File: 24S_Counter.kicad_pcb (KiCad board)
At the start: 2 copper layers, 0 parts

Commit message: Add unconnected files
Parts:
- added H1: MountingHole, MountingHole:MountingHole_2.2mm_M2, F.Cu at (47.5, 55.0)
- added H2: MountingHole, MountingHole:MountingHole_2.2mm_M2, F.Cu at (128.5, 55.0)
- added H3: MountingHole, MountingHole:MountingHole_2.2mm_M2, F.Cu at (47.5, 125.5)
- added H4: MountingHole, MountingHole:MountingHole_2.2mm_M2, F.Cu at (128.5, 125.5)
- added J1: +5V, my_footprints:Terminal_Block_5mm, F.Cu at (58.9, 61.0)
- added J2: EXT_CLK, Connector_PinHeader_2.54mm:PinHeader_1x02_P2.54mm_Vertical, F.Cu at (53.9, 106.6)
- added R1: 100R, Resistor_SMD:R_1206_3216Metric_Pad1.30x1.75mm_HandSolder, F.Cu at (87.9, 78.1)
- added R10: 100R, Resistor_SMD:R_1206_3216Metric_Pad1.30x1.75mm_HandSolder, F.Cu at (120.9, 111.6)
- added R11: 100R, Resistor_SMD:R_1206_3216Metric_Pad1.30x1.75mm_HandSolder, F.Cu at (120.9, 115.6)
- added R12: 100R, Resistor_SMD:R_1206_3216Metric_Pad1.30x1.75mm_HandSolder, F.Cu at (120.9, 120.1)
- added R13: 100R, Resistor_SMD:R_1206_3216Metric_Pad1.30x1.75mm_HandSolder, F.Cu at (117.4, 67.6)
- added R14: 100R, Resistor_SMD:R_1206_3216Metric_Pad1.30x1.75mm_HandSolder, F.Cu at (111.9, 67.6)
- added R15: 1K, Resistor_SMD:R_1206_3216Metric_Pad1.30x1.75mm_HandSolder, F.Cu at (76.4, 118.6)
- added R16: 10K, Resistor_SMD:R_1206_3216Metric_Pad1.30x1.75mm_HandSolder, F.Cu at (76.4, 113.1)
- added R17: 1K, Resistor_SMD:R_1206_3216Metric_Pad1.30x1.75mm_HandSolder, F.Cu at (60.9, 111.1)
- added R18: 10K, Resistor_SMD:R_1206_3216Metric_Pad1.30x1.75mm_HandSolder, F.Cu at (60.9, 104.7)
- added R2: 100R, Resistor_SMD:R_1206_3216Metric_Pad1.30x1.75mm_HandSolder, F.Cu at (87.9, 82.1)
- added R3: 100R, Resistor_SMD:R_1206_3216Metric_Pad1.30x1.75mm_HandSolder, F.Cu at (87.9, 86.1)
- added R4: 100R, Resistor_SMD:R_1206_3216Metric_Pad1.30x1.75mm_HandSolder, F.Cu at (87.9, 90.1)
- added R5: 100R, Resistor_SMD:R_1206_3216Metric_Pad1.30x1.75mm_HandSolder, F.Cu at (87.9, 94.1)
- added R6: 100R, Resistor_SMD:R_1206_3216Metric_Pad1.30x1.75mm_HandSolder, F.Cu at (96.9, 67.6)
- added R7: 100R, Resistor_SMD:R_1206_3216Metric_Pad1.30x1.75mm_HandSolder, F.Cu at (87.9, 74.1)
- added R8: 100R, Resistor_SMD:R_1206_3216Metric_Pad1.30x1.75mm_HandSolder, F.Cu at (120.9, 102.6)
- added R9: 100R, Resistor_SMD:R_1206_3216Metric_Pad1.30x1.75mm_HandSolder, F.Cu at (120.9, 107.1)
- added SW1: EN, my_footprints:slide_switch_2.54mm, F.Cu at (68.4, 108.1)
- added SW2: RST, my_footprints:tact_switch_5mm, F.Cu at (77.4, 105.1)
- added U1: 74LS192, my_footprints:74LS192, F.Cu at (58.1, 82.5)
- added U2: 74LS192, my_footprints:74LS192, F.Cu at (93.1, 111.8)
- added U3: 74LS48, my_footprints:74LS48, F.Cu at (72.9, 82.6)
- added U4: 74LS48, my_footprints:74LS48, F.Cu at (107.6, 111.4)
- added U5: SM420561N, Display_7Segment:7SegmentLED_LTS6760_LTS6780, F.Cu at (95.8, 90.2)
- added U6: SM420561N, Display_7Segment:7SegmentLED_LTS6760_LTS6780, F.Cu at (113.3, 90.1)

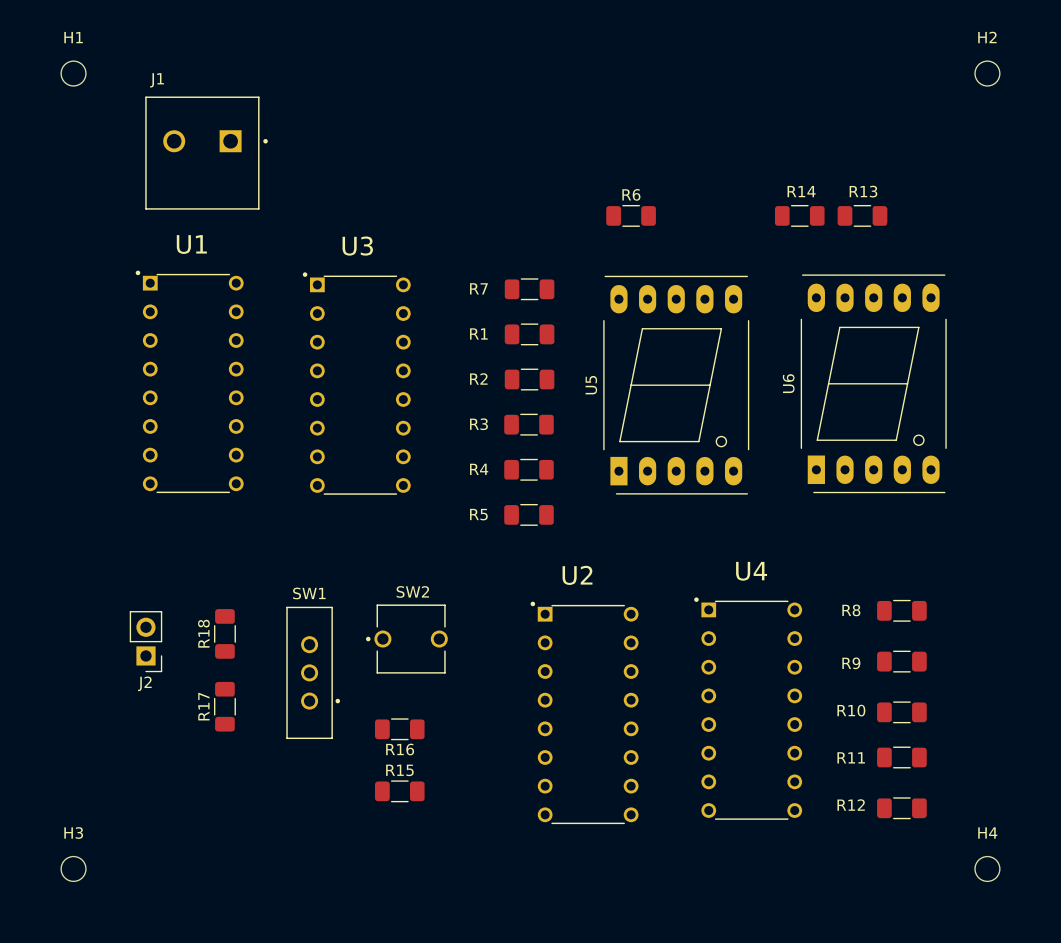
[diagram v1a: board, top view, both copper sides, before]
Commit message: Added all connections
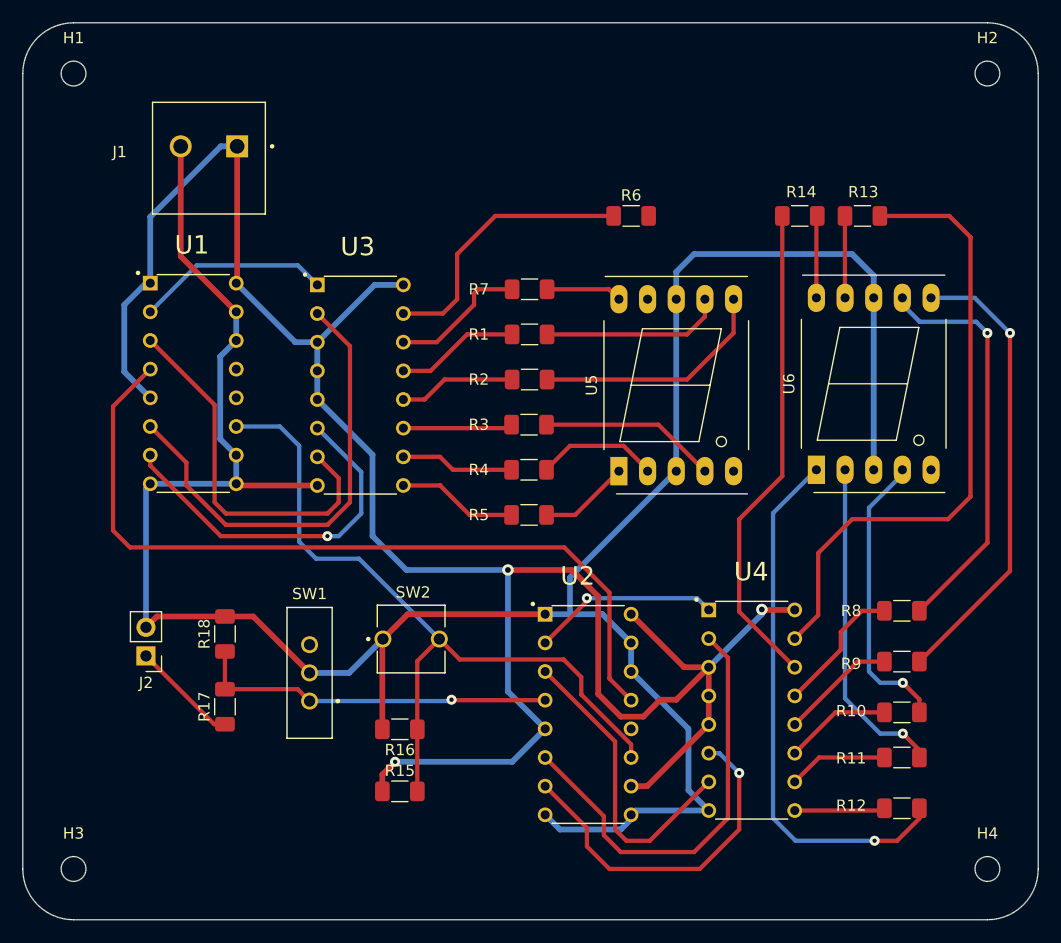
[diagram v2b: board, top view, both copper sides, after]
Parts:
- moved J1 0.73 mm to (59.5, 61.5)
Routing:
- net GND: track 0.00 -> 221.6 mm
- net /+5V: track 0.00 -> 188.3 mm, vias 0 -> 3
- net /B0: track 0.00 -> 72.3 mm
- net /Load: track 0.00 -> 68.0 mm
- net Net-(U4-f): track 0.00 -> 55.8 mm
- net Net-(U6-E): track 0.00 -> 48.0 mm, vias 0 -> 1
- net Net-(U4-g): track 0.00 -> 43.6 mm
- net Net-(U1-QC): track 0.00 -> 41.3 mm
- net Net-(U6-B): track 0.00 -> 40.7 mm, vias 0 -> 1
- net Net-(U2-QC): track 0.00 -> 38.5 mm
- net Net-(U6-A): track 0.00 -> 36.3 mm, vias 0 -> 1
- net Net-(U1-QA): track 0.00 -> 33.3 mm
- net /CLK: track 0.00 -> 32.2 mm, vias 0 -> 1
- net Net-(U1-QD): track 0.00 -> 32.2 mm, vias 0 -> 1
- net Net-(U2-QD): track 0.00 -> 31.1 mm, vias 0 -> 1
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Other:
- board outline added: 90 x 79.5 mm

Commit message: Finalize PCB
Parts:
- added G***: LOGO, logo:lance_logo_medium, F.Cu at (90.5, 59.0)
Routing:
- net Net-(U5-F): track 0.00 -> 7.42 mm
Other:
- board text added: "24 SECOND COUNTER"
- board text added: "Design Engineer: Salanap, Lance Kelly D. Date: 13 Apr 2026"
